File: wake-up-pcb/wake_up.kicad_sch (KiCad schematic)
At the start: 17 parts, among them J1 ESP32, J2 Screen, J3 Wireless control, J4 DS3231, J5 Conn_01x02, J6 Relay, Q1 2N3906, U1 NE555P

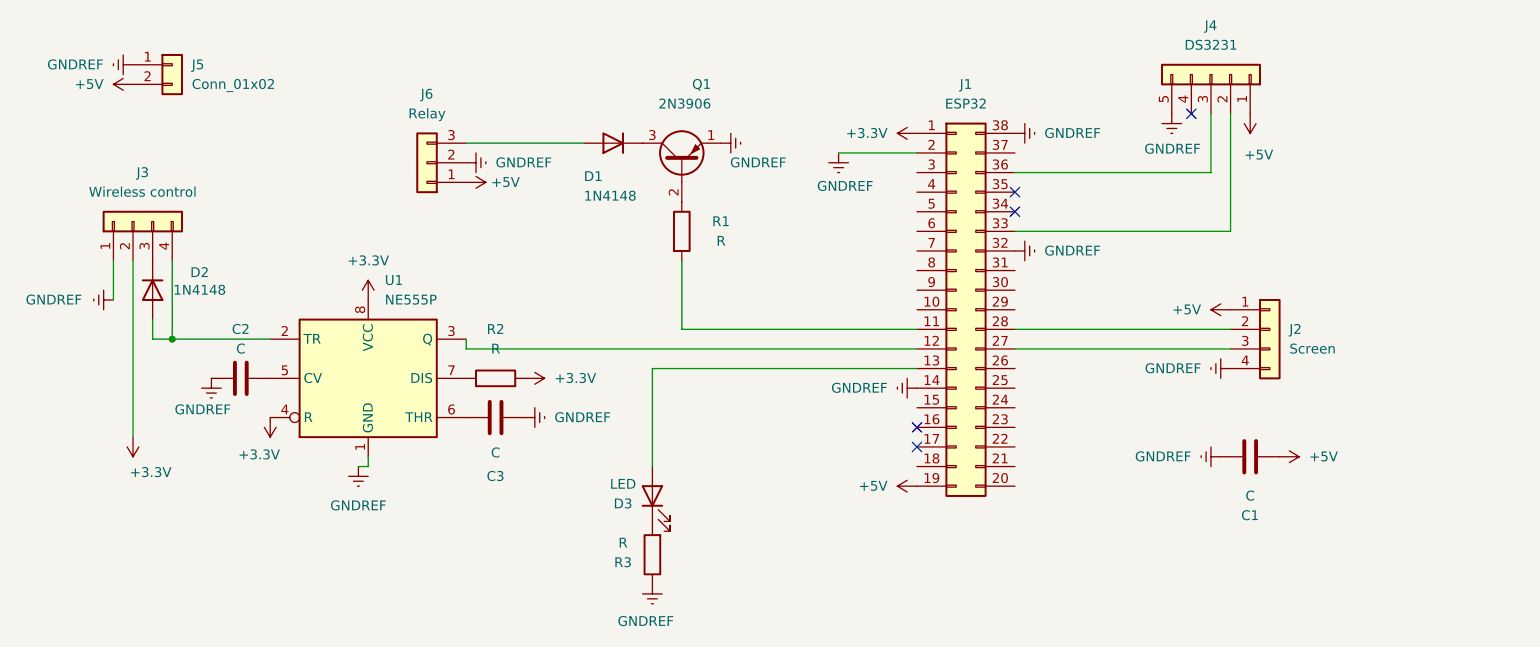
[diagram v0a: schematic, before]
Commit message: refactor(schematic): updated component layout, improved connections, and enhanced readability. Upgraded to KiCad E.D.A. 10.0.3.
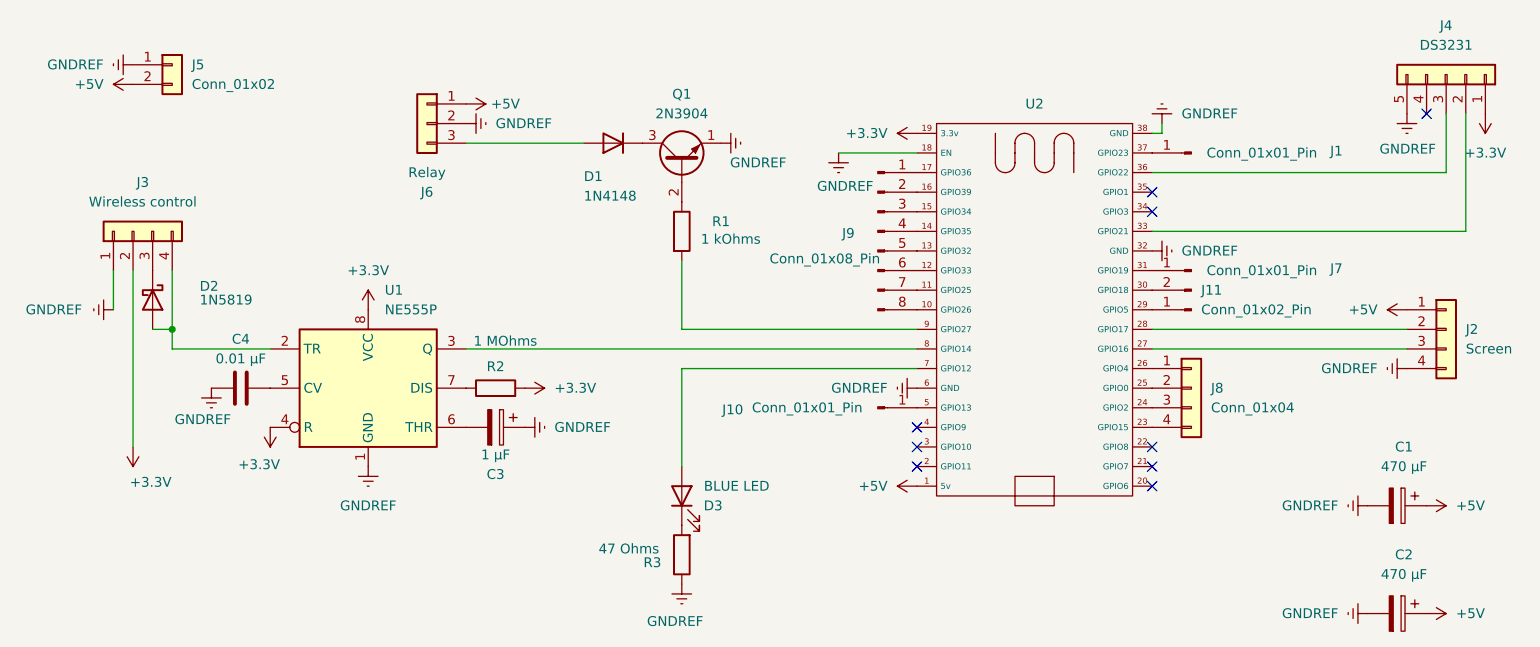
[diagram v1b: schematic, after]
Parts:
- removed C1, C3: C, symbol Device:C
- removed D2: 1N4148, Diode_THT:D_DO-35_SOD27_P7.62mm_Horizontal, symbol Diode:1N4148
- removed J1: ESP32, Module:Arduino_Nano, symbol Connector_Generic:Conn_02x19_Counter_Clockwise
- removed Q1: 2N3906, Package_TO_SOT_THT:TO-92_Inline, symbol Transistor_BJT:2N3906
- added C1, C2: 470 µF, Capacitor_THT:CP_Radial_D6.3mm_P2.50mm, symbol Device:C_Polarized
- added C3: 1 µF, Capacitor_THT:CP_Radial_D4.0mm_P2.00mm, symbol Device:C_Polarized
- added D2: 1N5819, Diode_THT:D_DO-41_SOD81_P7.62mm_Horizontal, symbol Diode:1N5819
- added J1, J10, J7: Conn_01x01_Pin, Connector_PinSocket_2.54mm:PinSocket_1x01_P2.54mm_Vertical, symbol Connector:Conn_01x01_Pin
- added J11: Conn_01x02_Pin, Connector_PinSocket_2.54mm:PinSocket_1x02_P2.54mm_Vertical, symbol Connector:Conn_01x02_Pin
- added J8: Conn_01x04, Connector_PinSocket_2.54mm:PinSocket_1x04_P2.54mm_Vertical, symbol Connector_Generic:Conn_01x04
- added J9: Conn_01x08_Pin, Connector_PinSocket_2.54mm:PinSocket_1x08_P2.54mm_Vertical, symbol Connector:Conn_01x08_Pin
- added Q1: 2N3904, Package_TO_SOT_THT:TO-92_Inline, symbol Transistor_BJT:2N3904
- added U2: (no value), Espressif:ESP32-DevKitC, symbol esp32_38pin:ESP32_38Pin
- C4: renamed from C2; value C -> 0.01 µF; footprint (none) -> Capacitor_THT:C_Disc_D9.0mm_W2.5mm_P5.00mm
- D3: value LED -> BLUE LED; footprint (none) -> LED_THT:LED_D5.0mm
- J2, J3: footprint (none) -> Connector_PinHeader_2.54mm:PinHeader_1x04_P2.54mm_Vertical
- J4: footprint Package_SO:SOIC-8_3.9x4.9mm_P1.27mm -> Connector_PinHeader_2.54mm:PinHeader_1x05_P2.54mm_Vertical
- J5: footprint (none) -> Connector_Wire:SolderWire-0.127sqmm_1x02_P3.7mm_D0.48mm_OD1mm
- J6: footprint (none) -> Connector_PinSocket_2.54mm:PinSocket_1x03_P2.54mm_Vertical
- R1: value R -> 1 kOhms; footprint (none) -> Resistor_THT:R_Axial_DIN0204_L3.6mm_D1.6mm_P7.62mm_Horizontal
- R2: value R -> 1 MOhms; footprint (none) -> Resistor_THT:R_Axial_DIN0204_L3.6mm_D1.6mm_P7.62mm_Horizontal
- R3: value R -> 47 Ohms; footprint (none) -> Resistor_THT:R_Axial_DIN0204_L3.6mm_D1.6mm_P7.62mm_Horizontal
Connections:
- net +3.3V: now also J4.1 (Pin_1), U2.19 (3.3v)
- net +5V: now also C1.1, C2.1, U2.1 (5v); no longer J4.1 (Pin_1)
- net GNDREF: now also C1.2, C2.2, C3.1, Q1.1 (E), U2.18 (EN), U2.32 (GND), U2.38 (GND), U2.6 (GND)
- net at R1.1: now also Q1.2 (B)
- net at R1.2: now also U2.9 (GPIO27)
- net at U1.6 (THR): now also C3.2
- net at J3.3 (Pin_3): now also D2.1 (K)
- net at J3.4 (Pin_4), U1.2 (TR): now also D2.2 (A)
- net at J4.2 (Pin_2): now also U2.33 (GPIO21)
- net at J4.3 (Pin_3): now also U2.36 (GPIO22)
- net at D1.1 (K): now also Q1.3 (C)
- net at U1.3 (Q): now also U2.8 (GPIO14)
- net at D3.2 (A): now also U2.7 (GPIO12)
- net at J2.3 (Pin_3): now also U2.27 (GPIO16)
- net at J2.2 (Pin_2): now also U2.28 (GPIO17)
- new net: J9.1 (Pin_1), U2.17 (GPIO36)
- new net: J9.2 (Pin_2), U2.16 (GPIO39)
- new net: J9.3 (Pin_3), U2.15 (GPIO34)
- new net: J9.4 (Pin_4), U2.14 (GPIO35)
- new net: J9.5 (Pin_5), U2.13 (GPIO32)
- new net: J9.6 (Pin_6), U2.12 (GPIO33)
- new net: J9.7 (Pin_7), U2.11 (GPIO25)
- new net: J9.8 (Pin_8), U2.10 (GPIO26)
- new net: J8.4 (Pin_4), U2.23 (GPIO15)
- new net: J8.3 (Pin_3), U2.24 (GPIO2)
- new net: J8.2 (Pin_2), U2.25 (GPIO0)
- new net: J8.1 (Pin_1), U2.26 (GPIO4)
- new net: J11.1 (Pin_1), U2.29 (GPIO5)
- new net: J11.2 (Pin_2), U2.30 (GPIO18)
- new net: J7.1 (Pin_1), U2.31 (GPIO19)
- new net: J1.1 (Pin_1), U2.37 (GPIO23)
- new net: J10.1 (Pin_1), U2.5 (GPIO13)
- no-connect marks 5 -> 9
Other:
- moved on the sheet: C4, D3, J2, J3, J4, J6, R2, R3, U1
